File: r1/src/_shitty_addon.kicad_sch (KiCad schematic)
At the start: 6 parts, among them J7 2x03-socket-2.54-through-board

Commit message: Assign MPN's and LCSC part numbers
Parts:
- D11, D12, D17, D18, D19: LCSC (none) -> C261278
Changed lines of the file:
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@@
+      (effects (font (size 1.27 1.27)) hide)
+    )
+    (property "LCSC" "C261278" (at 134.62 110.49 0)
       (effects (font (size 1.27 1.27)) hide)
     )
@@
       (effects (font (size 1.27 1.27)) hide)
     )
+    (property "LCSC" "C261278" (at 144.78 110.49 0)
+      (effects (font (size 1.27 1.27)) hide)
+    )
     (pin "1")
     (pin "2")
@@
     )
     (property "MPN" "ESD5Z5.0VC" (at 153.67 110.49 90)
+      (effects (font (size 1.27 1.27)) hide)
+    )
+    (property "LCSC" "C261278" (at 153.67 110.49 0)
       (effects (font (size 1.27 1.27)) hide)
     )
@@
       (effects (font (size 1.27 1.27)) hide)
     )
+    (property "LCSC" "C261278" (at 161.29 110.49 0)
+      (effects (font (size 1.27 1.27)) hide)
+    )
     (pin "1")
     (pin "2")
@@
       (effects (font (size 1.27 1.27)) hide)
     )
+    (property "LCSC" "C261278" (at 170.18 110.49 0)
+      (effects (font (size 1.27 1.27)) hide)
+    )

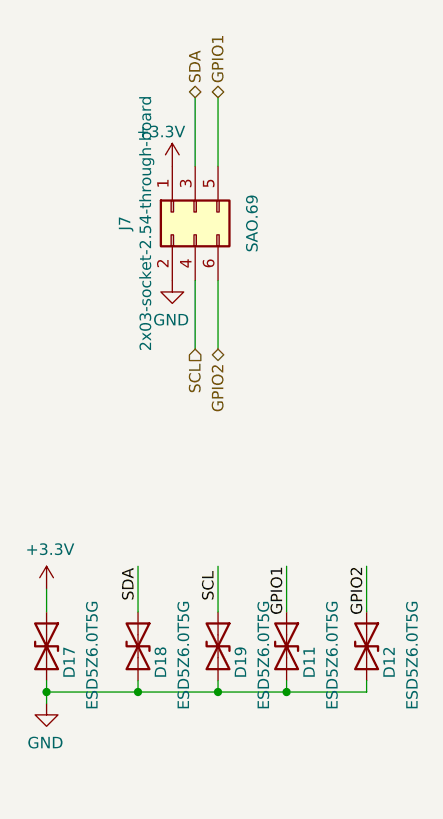
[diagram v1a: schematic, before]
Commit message: Reannotate component refs
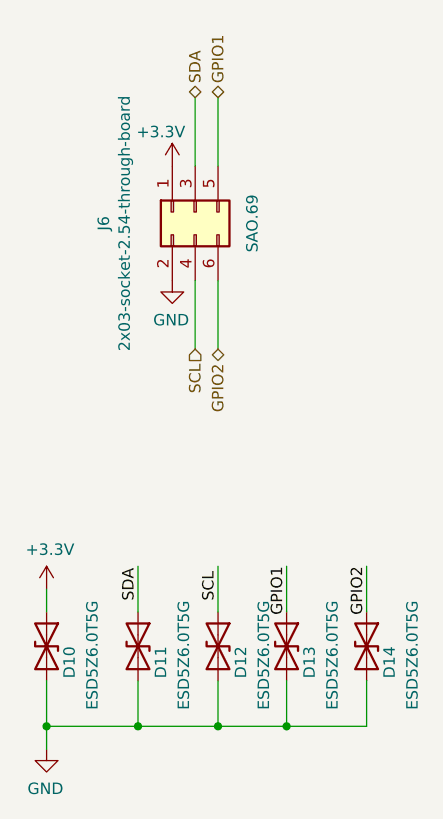
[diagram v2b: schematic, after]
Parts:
- renumbered D17 to D10, D18 to D11, D19 to D12, D11 to D13, D12 to D14, J7 to J6
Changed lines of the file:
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@@
 (kicad_sch (version 20230221) (generator eeschema)
   (paper "A4")
-  (junction (at 153.67 115.57) (diameter 0) (color 0 0 0 0)
-  )
-  (junction (at 144.78 115.57) (diameter 0) (color 0 0 0 0)
-  )
-  (junction (at 161.29 115.57) (diameter 0) (color 0 0 0 0)
-  )
-  (junction (at 134.62 115.57) (diameter 0) (color 0 0 0 0)
-  )
-  (wire (pts (xy 134.62 115.57) (xy 134.62 114.3))
-    (stroke (width 0) (type default))
-  )
-  (wire (pts (xy 144.78 115.57) (xy 153.67 115.57))
+  (junction (at 153.67 119.38) (diameter 0) (color 0 0 0 0)
+  )
+  (junction (at 144.78 119.38) (diameter 0) (color 0 0 0 0)
+  )
+  (junction (at 161.29 119.38) (diameter 0) (color 0 0 0 0)
+  )
+  (junction (at 134.62 119.38) (diameter 0) (color 0 0 0 0)
+  )
+  (wire (pts (xy 134.62 119.38) (xy 134.62 114.3))
+    (stroke (width 0) (type default))
+  )
+  (wire (pts (xy 144.78 119.38) (xy 153.67 119.38))
     (stroke (width 0) (type default))
   )
@@
     (stroke (width 0) (type default))
   )
-  (wire (pts (xy 161.29 115.57) (xy 170.18 115.57))
-    (stroke (width 0) (type default))
-  )
-  (wire (pts (xy 144.78 114.3) (xy 144.78 115.57))
+  (wire (pts (xy 161.29 119.38) (xy 170.18 119.38))
+    (stroke (width 0) (type default))
+  )
+  (wire (pts (xy 144.78 114.3) (xy 144.78 119.38))
     (stroke (width 0) (type default))
   )
@@
     (stroke (width 0) (type default))
   )
-  (wire (pts (xy 161.29 115.57) (xy 161.29 114.3))
-    (stroke (width 0) (type default))
-  )
-  (wire (pts (xy 153.67 115.57) (xy 161.29 115.57))
+  (wire (pts (xy 161.29 119.38) (xy 161.29 114.3))
+    (stroke (width 0) (type default))
+  )
+  (wire (pts (xy 153.67 119.38) (xy 161.29 119.38))
     (stroke (width 0) (type default))
   )
@@
     (stroke (width 0) (type default))
   )
-  (wire (pts (xy 170.18 115.57) (xy 170.18 114.3))
+  (wire (pts (xy 170.18 119.38) (xy 170.18 114.3))
     (stroke (width 0) (type default))
   )
@@
     (stroke (width 0) (type default))
   )
-  (wire (pts (xy 134.62 115.57) (xy 144.78 115.57))
-    (stroke (width 0) (type default))
-  )
-  (wire (pts (xy 153.67 115.57) (xy 153.67 114.3))
+  (wire (pts (xy 134.62 119.38) (xy 144.78 119.38))
+    (stroke (width 0) (type default))
+  )
+  (wire (pts (xy 153.67 119.38) (xy 153.67 114.3))
     (stroke (width 0) (type default))
   )
@@
     (stroke (width 0) (type default))
   )
-  (wire (pts (xy 134.62 116.84) (xy 134.62 115.57))
+  (wire (pts (xy 134.62 121.92) (xy 134.62 119.38))
     (stroke (width 0) (type default))
   )
@@
   (symbol (lib_id "Connector_Generic:Conn_02x03_Odd_Even") (at 151.13 62.23 90) (mirror x) (unit 1)
     (in_bom yes) (on_board yes) (dnp no)
-    (property "Reference" "J7" (at 143.3322 63.5 0)
-      (effects (font (size 1.27 1.27)))
-    )
-    (property "Value" "2x03-socket-2.54-through-board" (at 145.6436 63.5 0)
+    (property "Reference" "J6" (at 140.97 63.5 0)
+      (effects (font (size 1.27 1.27)))
+    )
+    (property "Value" "2x03-socket-2.54-through-board" (at 143.2814 63.5 0)
       (effects (font (size 1.27 1.27)))
     )
@@
       (project "tr23-badge-r1"
         (path "/ab725fe7-4504-40ef-b6af-82d065d00fb6/00000000-0000-0000-0000-00005dcc33e4"
-          (reference "J7") (unit 1)
+          (reference "J6") (unit 1)
         )
         (path "/ab725fe7-4504-40ef-b6af-82d065d00fb6"
@@
   (symbol (lib_id "power:GND") (at 148.59 69.85 0) (mirror y) (unit 1)
     (in_bom yes) (on_board yes) (dnp no)
-    (property "Reference" "#PWR075" (at 148.59 76.2 0)
+    (property "Reference" "#PWR070" (at 148.59 76.2 0)
       (effects (font (size 1.27 1.27)) hide)
     )
@@
       (project "tr23-badge-r1"
         (path "/ab725fe7-4504-40ef-b6af-82d065d00fb6/00000000-0000-0000-0000-00005dcc33e4"
-          (reference "#PWR075") (unit 1)
+          (reference "#PWR070") (unit 1)
         )
         (path "/ab725fe7-4504-40ef-b6af-82d065d00fb6"
@@
   (symbol (lib_id "power:+3.3V") (at 148.59 57.15 0) (unit 1)
     (in_bom yes) (on_board yes) (dnp no)
-    (property "Reference" "#PWR074" (at 148.59 60.96 0)
+    (property "Reference" "#PWR069" (at 148.59 60.96 0)
       (effects (font (size 1.27 1.27)) hide)
     )
@@
       (project "tr23-badge-r1"
         (path "/ab725fe7-4504-40ef-b6af-82d065d00fb6/00000000-0000-0000-0000-00005dcc33e4"
-          (reference "#PWR074") (unit 1)
+          (reference "#PWR069") (unit 1)
         )
         (path "/ab725fe7-4504-40ef-b6af-82d065d00fb6"
@@
   (symbol (lib_id "Device:D_TVS") (at 134.62 110.49 270) (unit 1)
     (in_bom yes) (on_board yes) (dnp no)
-    (property "Reference" "D17" (at 137.16 110.49 0)
+    (property "Reference" "D10" (at 137.16 110.49 0)
       (effects (font (size 1.27 1.27)) (justify left))
     )
@@
       (project "tr23-badge-r1"
         (path "/ab725fe7-4504-40ef-b6af-82d065d00fb6/00000000-0000-0000-0000-00005dcc33e4"
-          (reference "D17") (unit 1)
+          (reference "D10") (unit 1)
         )
         (path "/ab725fe7-4504-40ef-b6af-82d065d00fb6"
@@
   (symbol (lib_id "Device:D_TVS") (at 144.78 110.49 270) (unit 1)
     (in_bom yes) (on_board yes) (dnp no)
-    (property "Reference" "D18" (at 147.32 110.49 0)
+    (property "Reference" "D11" (at 147.32 110.49 0)
       (effects (font (size 1.27 1.27)) (justify left))
     )
@@
       (project "tr23-badge-r1"
         (path "/ab725fe7-4504-40ef-b6af-82d065d00fb6/00000000-0000-0000-0000-00005dcc33e4"
-          (reference "D18") (unit 1)
+          (reference "D11") (unit 1)
         )
         (path "/ab725fe7-4504-40ef-b6af-82d065d00fb6"
@@
   (symbol (lib_id "Device:D_TVS") (at 153.67 110.49 270) (unit 1)
     (in_bom yes) (on_board yes) (dnp no)
-    (property "Reference" "D19" (at 156.21 110.49 0)
+    (property "Reference" "D12" (at 156.21 110.49 0)
       (effects (font (size 1.27 1.27)) (justify left))
     )
@@
       (project "tr23-badge-r1"
         (path "/ab725fe7-4504-40ef-b6af-82d065d00fb6/00000000-0000-0000-0000-00005dcc33e4"
-          (reference "D19") (unit 1)
+          (reference "D12") (unit 1)
         )
         (path "/ab725fe7-4504-40ef-b6af-82d065d00fb6"
@@
   (symbol (lib_id "power:+3.3V") (at 134.62 104.14 0) (unit 1)
     (in_bom yes) (on_board yes) (dnp no)
-    (property "Reference" "#PWR076" (at 134.62 107.95 0)
+    (property "Reference" "#PWR067" (at 134.62 107.95 0)
       (effects (font (size 1.27 1.27)) hide)
     )
@@
       (project "tr23-badge-r1"
         (path "/ab725fe7-4504-40ef-b6af-82d065d00fb6/00000000-0000-0000-0000-00005dcc33e4"
-          (reference "#PWR076") (unit 1)
+          (reference "#PWR067") (unit 1)
         )
         (path "/ab725fe7-4504-40ef-b6af-82d065d00fb6"
@@
     )
   )
-  (symbol (lib_id "power:GND") (at 134.62 116.84 0) (mirror y) (unit 1)
-    (in_bom yes) (on_board yes) (dnp no)
-    (property "Reference" "#PWR077" (at 134.62 123.19 0)
-      (effects (font (size 1.27 1.27)) hide)
-    )
-    (property "Value" "GND" (at 134.493 121.2342 0)
-      (effects (font (size 1.27 1.27)))
-    )
-    (property "Footprint" "" (at 134.62 116.84 0)
-      (effects (font (size 1.27 1.27)) hide)
-    )
-    (property "Datasheet" "" (at 134.62 116.84 0)
-      (effects (font (size 1.27 1.27)) hide)
-    )
-    (pin "1")
-    (instances
-      (project "tr23-badge-r1"
-        (path "/ab725fe7-4504-40ef-b6af-82d065d00fb6/00000000-0000-0000-0000-00005dcc33e4"
-          (reference "#PWR077") (unit 1)
+  (symbol (lib_id "power:GND") (at 134.62 121.92 0) (mirror y) (unit 1)
+    (in_bom yes) (on_board yes) (dnp no)
+    (property "Reference" "#PWR068" (at 134.62 128.27 0)
+      (effects (font (size 1.27 1.27)) hide)
+    )
+    (property "Value" "GND" (at 134.493 126.3142 0)
+      (effects (font (size 1.27 1.27)))
+    )
+    (property "Footprint" "" (at 134.62 121.92 0)
+      (effects (font (size 1.27 1.27)) hide)
+    )
+    (property "Datasheet" "" (at 134.62 121.92 0)
+      (effects (font (size 1.27 1.27)) hide)
+    )
+    (pin "1")
+    (instances
+      (project "tr23-badge-r1"
+        (path "/ab725fe7-4504-40ef-b6af-82d065d00fb6/00000000-0000-0000-0000-00005dcc33e4"
+          (reference "#PWR068") (unit 1)
         )
         (path "/ab725fe7-4504-40ef-b6af-82d065d00fb6"
@@
   (symbol (lib_id "Device:D_TVS") (at 161.29 110.49 270) (unit 1)
     (in_bom yes) (on_board yes) (dnp no)
-    (property "Reference" "D11" (at 163.83 110.49 0)
+    (property "Reference" "D13" (at 163.83 110.49 0)
       (effects (font (size 1.27 1.27)) (justify left))
     )
@@
       (project "tr23-badge-r1"
         (path "/ab725fe7-4504-40ef-b6af-82d065d00fb6/00000000-0000-0000-0000-00005dcc33e4"
-          (reference "D11") (unit 1)
+          (reference "D13") (unit 1)
         )
         (path "/ab725fe7-4504-40ef-b6af-82d065d00fb6"
@@
   (symbol (lib_id "Device:D_TVS") (at 170.18 110.49 270) (unit 1)
     (in_bom yes) (on_board yes) (dnp no)
-    (property "Reference" "D12" (at 172.72 110.49 0)
+    (property "Reference" "D14" (at 172.72 110.49 0)
       (effects (font (size 1.27 1.27)) (justify left))
     )
@@
       (project "tr23-badge-r1"
         (path "/ab725fe7-4504-40ef-b6af-82d065d00fb6/00000000-0000-0000-0000-00005dcc33e4"
-          (reference "D12") (unit 1)
-        )
-        (path "/ab725fe7-4504-40ef-b6af-82d065d00fb6"
+          (reference "D14") (unit 1)
+        )
+        (path "/ab725fe7-4504-40ef-b6af-82d065d00fb6"

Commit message: Assign footprints from jeffmakes-footprints lib
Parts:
- D10, D11, D12, D13, D14: footprint jeffmakes-footprints:SOD-523-numbered-pads -> jeffmakes_footprints:SOD-523-numbered-pads
- J6: footprint jeffmakes-footprints:PinSocket_2x03_P2.54mm_Through-Board-Mating -> jeffmakes_footprints:PinSocket_2x03_P2.54mm_Through-Board-Mating
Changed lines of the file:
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@@
       (effects (font (size 1.27 1.27)))
     )
-    (property "Footprint" "jeffmakes-footprints:PinSocket_2x03_P2.54mm_Through-Board-Mating" (at 151.13 62.23 0)
+    (property "Footprint" "jeffmakes_footprints:PinSocket_2x03_P2.54mm_Through-Board-Mating" (at 151.13 62.23 0)
       (effects (font (size 1.27 1.27)) hide)
     )
@@
       (effects (font (size 1.27 1.27)) (justify left))
     )
-    (property "Footprint" "jeffmakes-footprints:SOD-523-numbered-pads" (at 134.62 110.49 0)
+    (property "Footprint" "jeffmakes_footprints:SOD-523-numbered-pads" (at 134.62 110.49 0)
       (effects (font (size 1.27 1.27)) hide)
     )
@@
       (effects (font (size 1.27 1.27)) (justify left))
     )
-    (property "Footprint" "jeffmakes-footprints:SOD-523-numbered-pads" (at 144.78 110.49 0)
+    (property "Footprint" "jeffmakes_footprints:SOD-523-numbered-pads" (at 144.78 110.49 0)
       (effects (font (size 1.27 1.27)) hide)
     )
@@
       (effects (font (size 1.27 1.27)) (justify left))
     )
-    (property "Footprint" "jeffmakes-footprints:SOD-523-numbered-pads" (at 153.67 110.49 0)
+    (property "Footprint" "jeffmakes_footprints:SOD-523-numbered-pads" (at 153.67 110.49 0)
       (effects (font (size 1.27 1.27)) hide)
     )
@@
       (effects (font (size 1.27 1.27)) (justify left))
     )
-    (property "Footprint" "jeffmakes-footprints:SOD-523-numbered-pads" (at 161.29 110.49 0)
+    (property "Footprint" "jeffmakes_footprints:SOD-523-numbered-pads" (at 161.29 110.49 0)
       (effects (font (size 1.27 1.27)) hide)
     )
@@
       (effects (font (size 1.27 1.27)) (justify left))
     )
-    (property "Footprint" "jeffmakes-footprints:SOD-523-numbered-pads" (at 170.18 110.49 0)
-      (effects (font (size 1.27 1.27)) hide)
-    )
+    (property "Footprint" "jeffmakes_footprints:SOD-523-numbered-pads" (at 170.18 110.49 0)
+      (effects (font (size 1.27 1.27)) hide)
+    )

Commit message: ERC pass. Schematic complete.
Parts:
- D10, D11, D12, D13, D14: footprint jeffmakes_footprints:SOD-523-numbered-pads -> jeffmakes-footprints:SOD-523-numbered-pads
- J6: footprint jeffmakes_footprints:PinSocket_2x03_P2.54mm_Through-Board-Mating -> jeffmakes-footprints:PinSocket_2x03_P2.54mm_Through-Board-Mating
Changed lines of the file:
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@@
       (effects (font (size 1.27 1.27)))
     )
-    (property "Footprint" "jeffmakes_footprints:PinSocket_2x03_P2.54mm_Through-Board-Mating" (at 151.13 62.23 0)
+    (property "Footprint" "jeffmakes-footprints:PinSocket_2x03_P2.54mm_Through-Board-Mating" (at 151.13 62.23 0)
       (effects (font (size 1.27 1.27)) hide)
     )
@@
       (effects (font (size 1.27 1.27)) (justify left))
     )
-    (property "Footprint" "jeffmakes_footprints:SOD-523-numbered-pads" (at 134.62 110.49 0)
+    (property "Footprint" "jeffmakes-footprints:SOD-523-numbered-pads" (at 134.62 110.49 0)
       (effects (font (size 1.27 1.27)) hide)
     )
@@
       (effects (font (size 1.27 1.27)) (justify left))
     )
-    (property "Footprint" "jeffmakes_footprints:SOD-523-numbered-pads" (at 144.78 110.49 0)
+    (property "Footprint" "jeffmakes-footprints:SOD-523-numbered-pads" (at 144.78 110.49 0)
       (effects (font (size 1.27 1.27)) hide)
     )
@@
       (effects (font (size 1.27 1.27)) (justify left))
     )
-    (property "Footprint" "jeffmakes_footprints:SOD-523-numbered-pads" (at 153.67 110.49 0)
+    (property "Footprint" "jeffmakes-footprints:SOD-523-numbered-pads" (at 153.67 110.49 0)
       (effects (font (size 1.27 1.27)) hide)
     )
@@
       (effects (font (size 1.27 1.27)) (justify left))
     )
-    (property "Footprint" "jeffmakes_footprints:SOD-523-numbered-pads" (at 161.29 110.49 0)
+    (property "Footprint" "jeffmakes-footprints:SOD-523-numbered-pads" (at 161.29 110.49 0)
       (effects (font (size 1.27 1.27)) hide)
     )
@@
       (effects (font (size 1.27 1.27)) (justify left))
     )
-    (property "Footprint" "jeffmakes_footprints:SOD-523-numbered-pads" (at 170.18 110.49 0)
-      (effects (font (size 1.27 1.27)) hide)
-    )
+    (property "Footprint" "jeffmakes-footprints:SOD-523-numbered-pads" (at 170.18 110.49 0)
+      (effects (font (size 1.27 1.27)) hide)
+    )
